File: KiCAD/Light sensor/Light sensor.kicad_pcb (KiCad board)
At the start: 2 copper layers, 40 x 41.5 mm, 22 parts, among them J1 USB_B_Micro, U1 Opamp_Quad, U2 3.8V LDO, U3 1.024 Vref

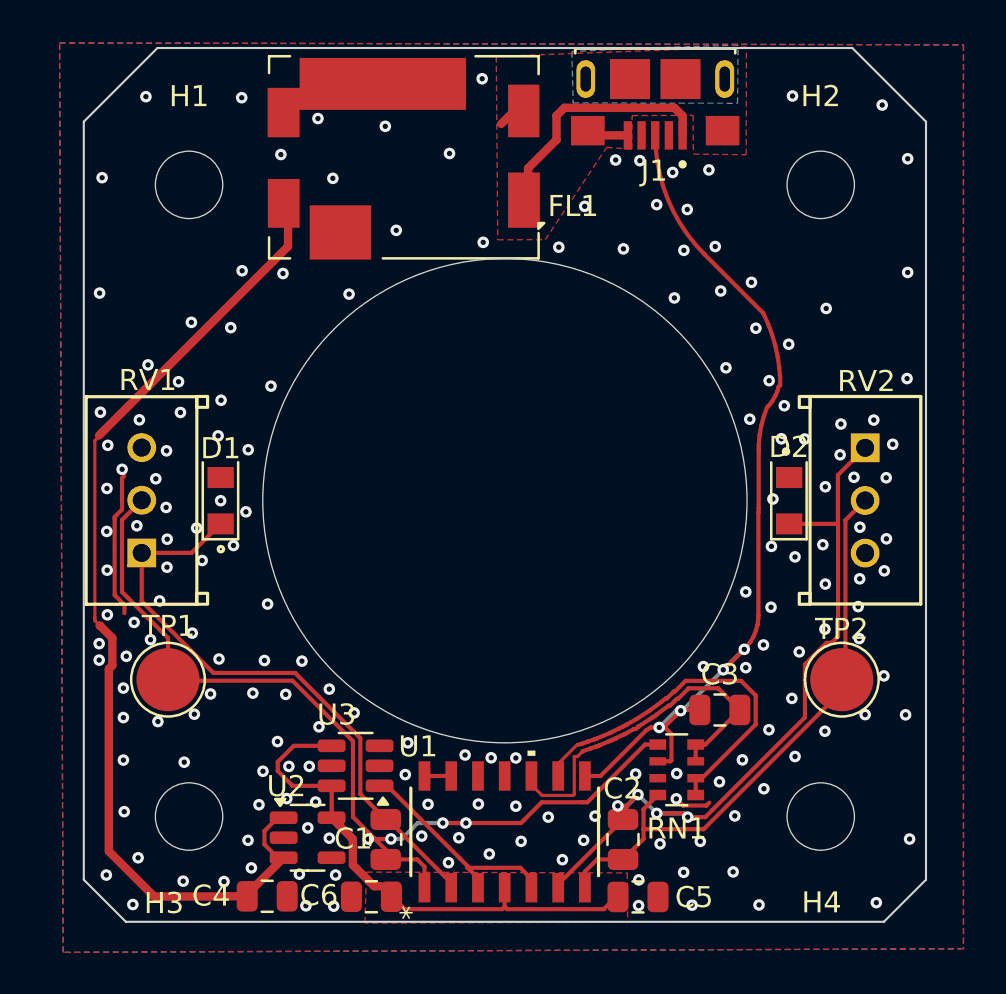
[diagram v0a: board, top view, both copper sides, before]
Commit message: Add offset to diff amp, swap for better photodiodes
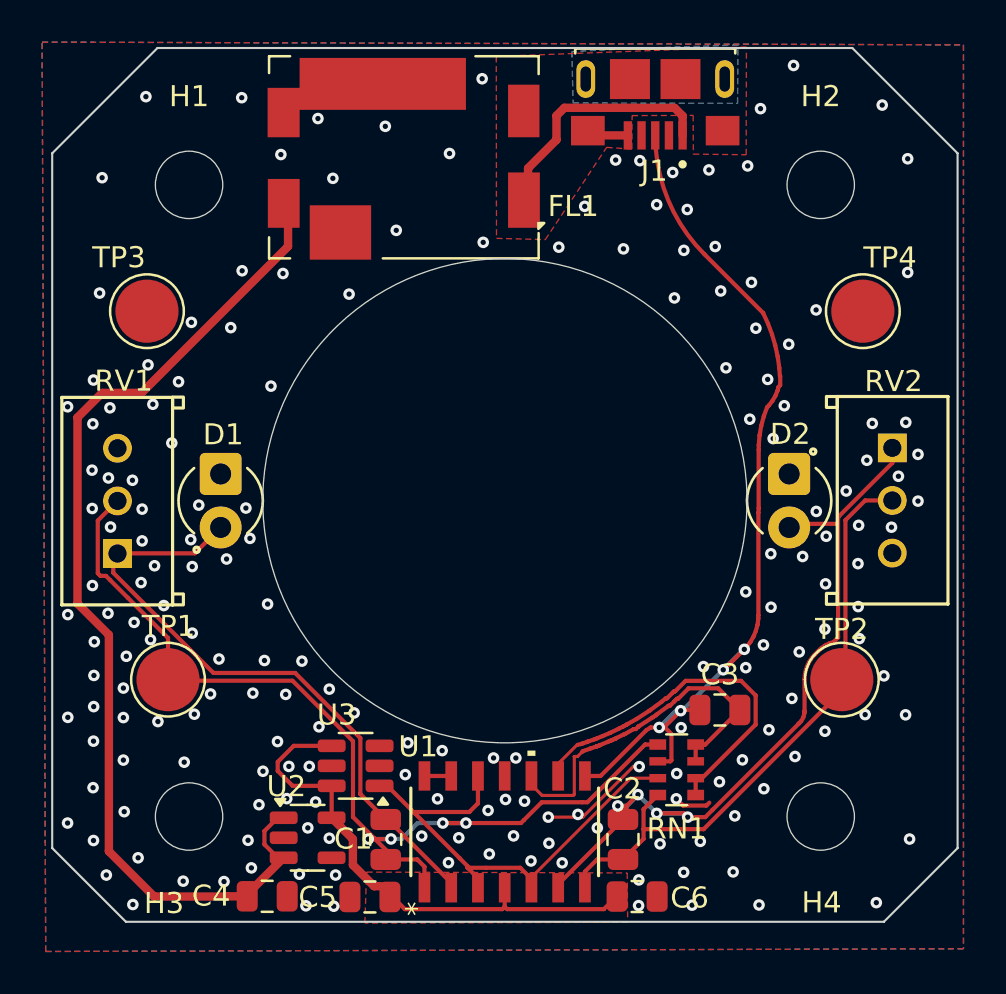
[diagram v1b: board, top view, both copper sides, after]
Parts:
- added TP3: TestPoint, TestPoint:TestPoint_Pad_D3.0mm, F.Cu at (-17.0, -9.00)
- added TP4: TestPoint, TestPoint:TestPoint_Pad_D3.0mm, F.Cu at (17.0, -9.00)
- D1, D2: footprint Custom:Photodiode -> Custom:XDCR_SFH_229
- RN1: value 1k, 10k -> 1k, 10k-10x Gain
- moved C5 12.7 mm to (-6.41, 18.8), turned to 180 degrees
- moved C6 12.6 mm to (6.28, 18.8), turned to 0 degrees
- moved RV2 1.29 mm to (18.4, -2.51)
- moved RV1 1.15 mm to (-18.4, 2.51)
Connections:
- RN1 pad 7: GND -> +1V0
- U1 pad 12: GND -> +1V0
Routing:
- net +1V0: track 11.2 -> 24.2 mm
- net GND: track 8.66 -> 6.99 mm, vias 181 -> 191
- net /Vd2: track 29.7 -> 31.0 mm
- net Net-(FL1-PSG): track 3.69 -> 2.41 mm
- net Net-(D1-K): track 29.5 -> 30.5 mm
- net /Vd1: track 48.8 -> 49.4 mm
- net +5V: track 49.4 -> 49.9 mm
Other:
- board size 40 x 41.5 mm -> 43 x 41.5 mm

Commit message: Add coax connector for Vout
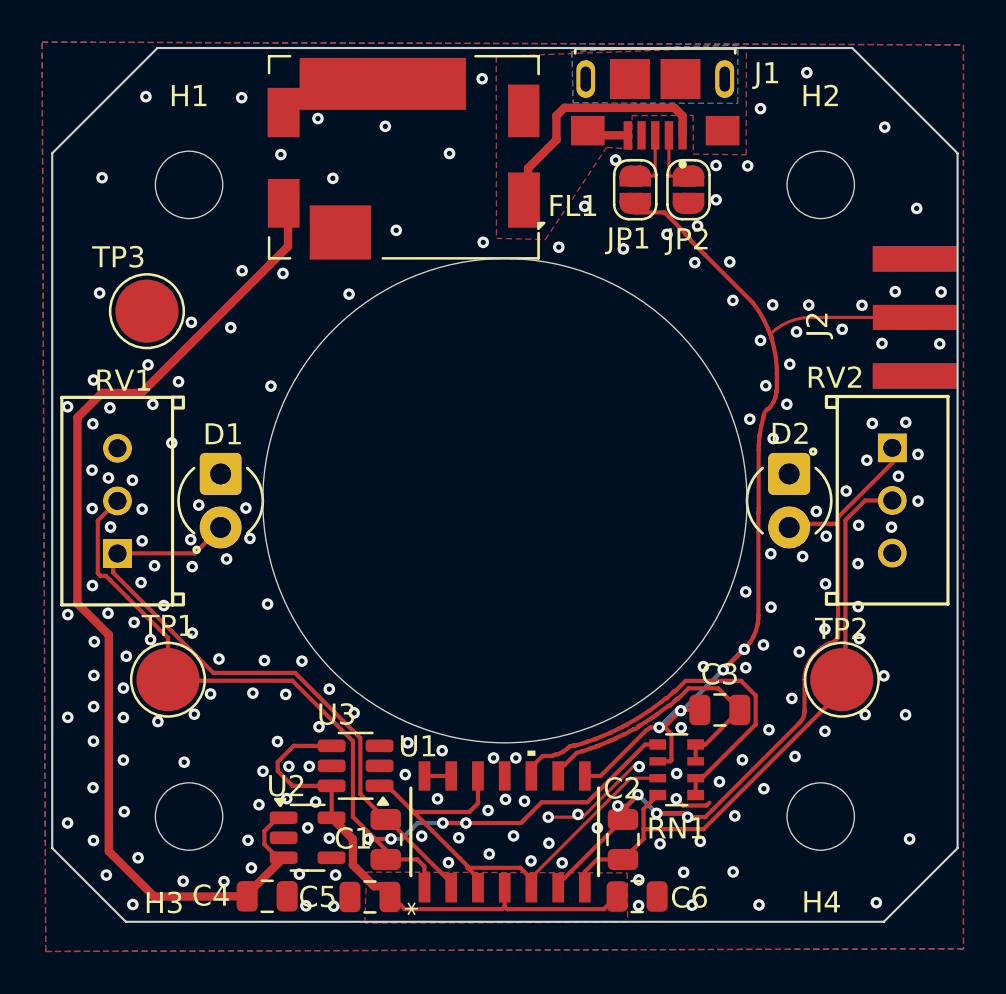
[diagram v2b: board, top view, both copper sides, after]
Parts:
- removed TP4: TestPoint, TestPoint:TestPoint_Pad_D3.0mm
- added J2: Conn_Coaxial, Custom:ADAMTECH_RF2-143-T-17-50-G, F.Cu at (21.5, -8.70)
- added JP1: Jumper_2_Open, Jumper:SolderJumper-2_P1.3mm_Open_RoundedPad1.0x1.5mm, F.Cu at (6.19, -14.8)
- added JP2: Jumper_2_Open, Jumper:SolderJumper-2_P1.3mm_Open_RoundedPad1.0x1.5mm, F.Cu at (8.72, -14.8)
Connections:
- J1 pad 2: GND -> Net-(J1-D-)
- J1 pad 3: /Vout -> Net-(J1-D+)
- U1 pad 10: Net-(RN1-R3.1) -> Net-(RN1-R1.1)
- U1 pad 9: Net-(RN1-R1.1) -> Net-(RN1-R3.1)
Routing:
- net /Vout: track 43.1 -> 48.5 mm
- net Net-(J1-D+): track 0.00 -> 2.88 mm
- net Net-(J1-D-): track 0.00 -> 2.86 mm
- net Net-(RN1-R3.1): track 17.4 -> 14.7 mm
- net Net-(RN1-R1.1): track 17.8 -> 19.3 mm
- net GND: vias 191 -> 194
